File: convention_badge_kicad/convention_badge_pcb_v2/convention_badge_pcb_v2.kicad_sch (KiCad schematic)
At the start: 23 parts, among them J1 USBC, J2 ER-CON24HT-1, J3 3.7V Battery, SW1 SW4X2, SW2 SW4X2, SW4 SW_SPST, U1 ESP32-C3-WROOM-02, U3 TP4056

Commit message: schematic minus e paper integration complete
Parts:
- added C5: 0.1uF, PCM_JLCPCB:C_0603, symbol EESD:C
- added C6, C8: 2.2uF, PCM_JLCPCB:C_0603, symbol Device:C_Small_US
- added C7: 100uF, PCM_JLCPCB:C_0603, symbol Device:C_Small_US
- added C9: 0.1uF, PCM_JLCPCB:C_0603, symbol Device:C_Small_US
- added D3: SS14, PCM_JLCPCB:D_DO-214AC(SMA), symbol Device:D
- added Q1: LP0404N3T5G, Package_TO_SOT_SMD:SOT-883, symbol Simulation_SPICE:PMOS
- added R10: 100k, PCM_JLCPCB:R_0603, symbol Device:R_Small_US
- added R9: 1k, PCM_JLCPCB:R_0603, symbol Device:R_US
- added SW3, SW4, SW5, SW7, SW8: SW_Push, Button_Switch_THT:SW_PUSH_6mm, symbol Switch:SW_Push
- added U2: FS8205A, Package_TO_SOT_SMD:SOT-23-6, symbol 3_Battery_Managment:FS8205A
- added U4: DW01A, Package_TO_SOT_SMD:SOT-23-6, symbol 3_Battery_Managment:DW10A
- added U5: TLV75733PDBV, Package_TO_SOT_SMD:SOT-23-5, symbol Regulator_Linear:TLV75733PDBV
- C1, C2, C3, C4: footprint EESD:C0603 -> PCM_JLCPCB:C_0603
- D1, D2: footprint (none) -> PCM_JLCPCB:D_0603
- DISP1: renamed from DISP; value EPaper Display -> EPaper Breakout
- J1: footprint (none) -> Connector_USB:USB_C_Receptacle_GCT_USB4105-xx-A_16P_TopMnt_Horizontal
- J2: value ER-CON24HT-1 -> EPaper
- R1, R2: footprint EESD:R0603 -> PCM_JLCPCB:R_0603
- R3, R4, R5, R6, R8: footprint (none) -> PCM_JLCPCB:R_0603
- R7: value 1.2k -> 10k; footprint (none) -> PCM_JLCPCB:R_0603
- SW1, SW2: footprint EESD:PB4X2 -> PCM_JLCPCB:SW-SMD_4P-L5.1-W5.1-P3.70-LS6.5-TL-2
- renumbered SW4 to SW6
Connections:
- net +3.3V: now also C8.1, C9.1, U5.5 (OUT)
- net +3.7V: now also C4.1, R8.2, SW6.1 (A), U3.5 (BAT), Q1.1 (D); no longer J3.1 (Pin_1), SW6.2 (B)
- net EN: now also SW1.4; no longer SW1.2
- net GND: now also C4.2, SW1.2, SW2.2, C6.2, C7.2, C8.2, C9.2, R10.2, SW3.2, SW4.2, SW5.2, SW7.2, SW8.2, U5.2 (GND); no longer SW1.4, SW2.4
- net GPIO3: now also SW8.1
- net GPIO9: now also SW2.4; no longer SW2.2
- net VUSB: now also C7.1, D3.2 (A), Q1.2 (G), R10.1
- net at R8.1: now also C5.1, U4.5 (VCC)
- net GPIO20: now reaches U1.11 (GPIO20/U0RXD)
- net GPIO20: now also SW5.1
- net GPIO21: now reaches U1.12 (GPIO21/U0TXD)
- net GPIO21: now also SW7.1
- net GPIO1: now reaches U1.17 (GPIO1/ADC1_CH1/XTAL_32K_N)
- net GPIO1: now also SW4.1
- net GPIO0: now reaches U1.18 (GPIO0/ADC1_CH0/XTAL_32K_P)
- net GPIO0: now also SW3.1
- net at J3.2 (Pin_2): now also C5.2, U2.3 (S2), U4.6 (GND)
- new net: R9.1, U2.1 (S1)
- new net: R9.2, U4.2 (VM)
- new net: C6.1, D3.1 (K), Q1.3 (S), U5.1 (IN), U5.3 (EN)
- new net: J3.1 (Pin_1), SW6.2 (B)
- new net: U2.4 (G2), U4.1 (OD)
- new net: U2.6 (G1), U4.3 (OC)
- no-connect marks 2 -> 3
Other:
- moved on the sheet: C2, C4, DISP1, J2, J3, R4, R8, SW6

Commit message: layout is almost complete, kind of a rats nest
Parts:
- removed J2: EPaper, eastrising:ER-CON24HT-1, symbol eastrising:ER-EPD029-1_FPC
- removed SW7, SW8: SW_Push, Button_Switch_THT:SW_PUSH_6mm, symbol Switch:SW_Push
- added C10: 10uF, PCM_JLCPCB:C_0603, symbol Device:C_Small_US
- added D4, D5: LED, LED_THT:LED_D5.0mm, symbol Device:LED
- added J4, J5: Conn_01x10_Pin, Connector_PinHeader_2.54mm:PinHeader_1x10_P2.54mm_Vertical, symbol Connector:Conn_01x10_Pin
- added R11, R12: 1k, PCM_JLCPCB:R_0603, symbol Device:R_US
- R10: value 100k -> 10k
- R7: value 10k -> 2.2k
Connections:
- net +3.3V: now also C10.1, J4.1 (Pin_1), J4.10 (Pin_10)
- net EN: now also J4.2 (Pin_2)
- net GND: now also C10.2, J4.9 (Pin_9), R11.2, R12.2
- net GPIO0: now also D4.2 (A), J5.2 (Pin_2); no longer SW3.1
- net GPIO1: now also D5.2 (A), J5.3 (Pin_3); no longer SW4.1
- net GPIO10: now also SW5.1, J5.10 (Pin_10)
- net GPIO2: now also J5.4 (Pin_4)
- net GPIO20: now also SW4.1, J5.9 (Pin_9); no longer SW5.1
- net GPIO21: now also SW3.1, J5.8 (Pin_8)
- net GPIO3: now also J5.5 (Pin_5)
- net GPIO4: now also J4.3 (Pin_3)
- net GPIO5: now also J4.4 (Pin_4)
- net GPIO6: now also J4.5 (Pin_5)
- net GPIO7: now also J4.6 (Pin_6)
- net GPIO8: now also J4.7 (Pin_7)
- net GPIO9: now also J4.8 (Pin_8)
- net USB_D+: now also J5.6 (Pin_6)
- net USB_D-: now also J5.7 (Pin_7)
- net VUSB: now also J5.1 (Pin_1)
- net +3.7V renamed VBAT
- new net: D5.1 (K), R12.1
- new net: D4.1 (K), R11.1
- no-connect marks 3 -> 5
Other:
- moved on the sheet: C3, C4, C5, C6, C7, C8, C9, D1, D2, D3, DISP1, J3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

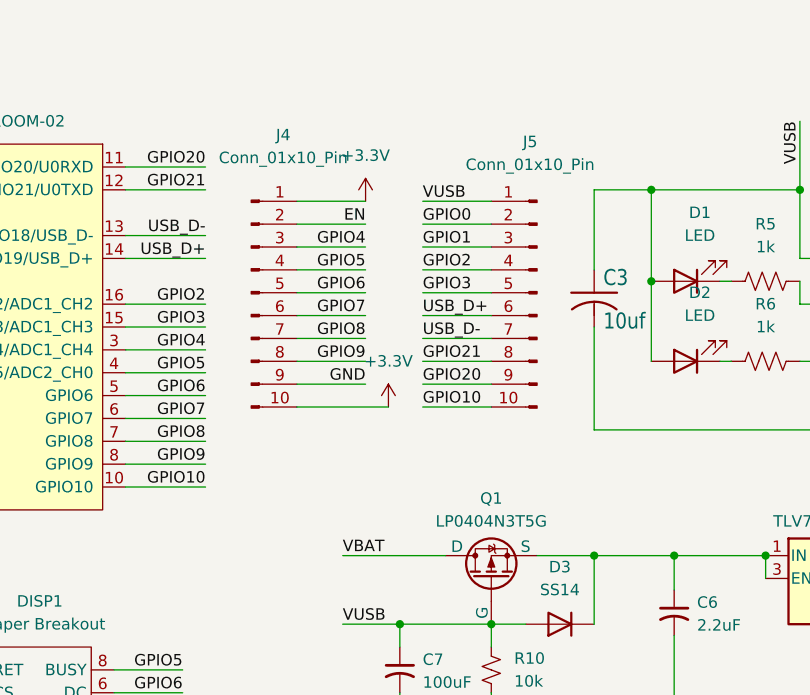
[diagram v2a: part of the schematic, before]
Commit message: cleaned up layout and seperated breakout headers.
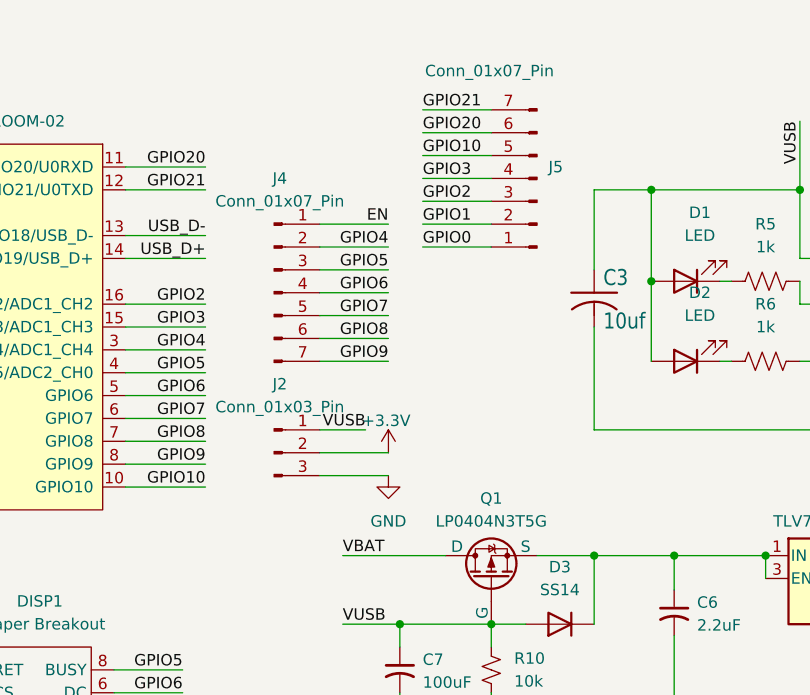
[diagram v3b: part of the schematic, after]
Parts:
- removed J4, J5: Conn_01x10_Pin, Connector_PinHeader_2.54mm:PinHeader_1x10_P2.54mm_Vertical, symbol Connector:Conn_01x10_Pin
- added J2: Conn_01x03_Pin, Connector_PinHeader_2.54mm:PinHeader_1x03_P2.54mm_Vertical, symbol Connector:Conn_01x03_Pin
- added J4, J5: Conn_01x07_Pin, Connector_PinHeader_2.54mm:PinHeader_1x07_P2.54mm_Vertical, symbol Connector:Conn_01x07_Pin
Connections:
- net +3.3V: now also J2.2 (Pin_2)
- net EN: now also J4.1 (Pin_1)
- net GND: now also J2.3 (Pin_3)
- net GPIO0: now also J5.1 (Pin_1)
- net GPIO1: now also J5.2 (Pin_2)
- net GPIO10: now also J5.5 (Pin_5)
- net GPIO2: now also J5.3 (Pin_3)
- net GPIO20: now also J5.6 (Pin_6)
- net GPIO21: now also J5.7 (Pin_7)
- net GPIO3: now also J5.4 (Pin_4)
- net GPIO4: now also J4.2 (Pin_2)
- net GPIO5: now also J4.3 (Pin_3)
- net GPIO6: now also J4.4 (Pin_4)
- net GPIO7: now also J4.5 (Pin_5)
- net GPIO8: now also J4.6 (Pin_6)
- net GPIO9: now also J4.7 (Pin_7)
- net VUSB: now also J2.1 (Pin_1)

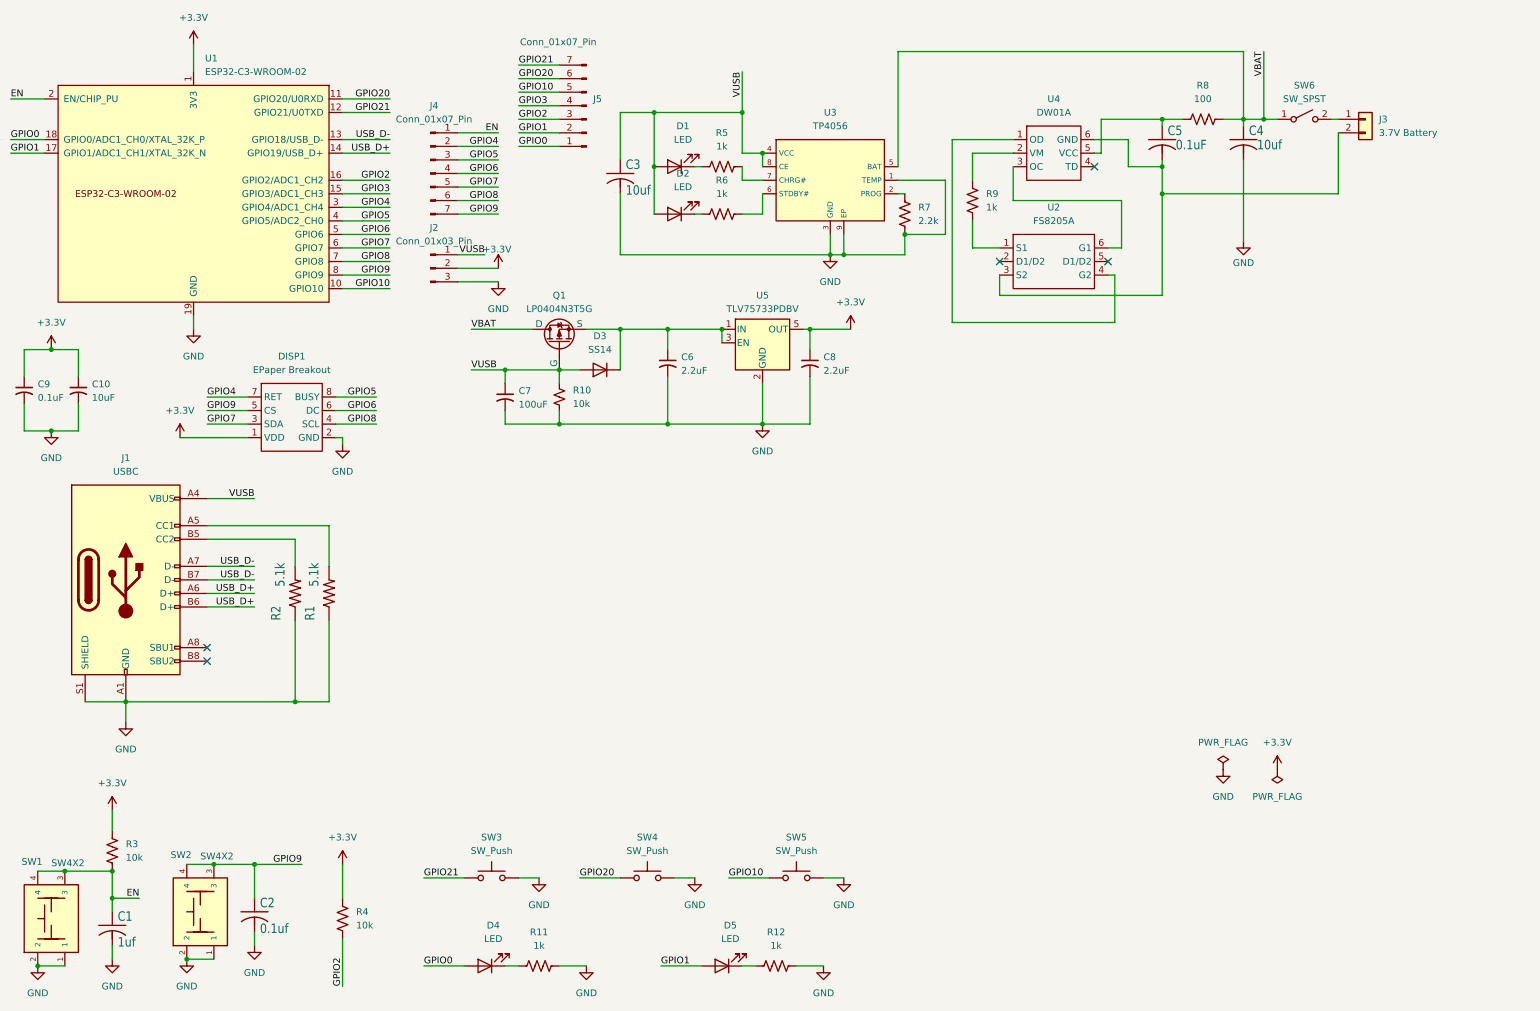
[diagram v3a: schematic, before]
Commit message: made board outline
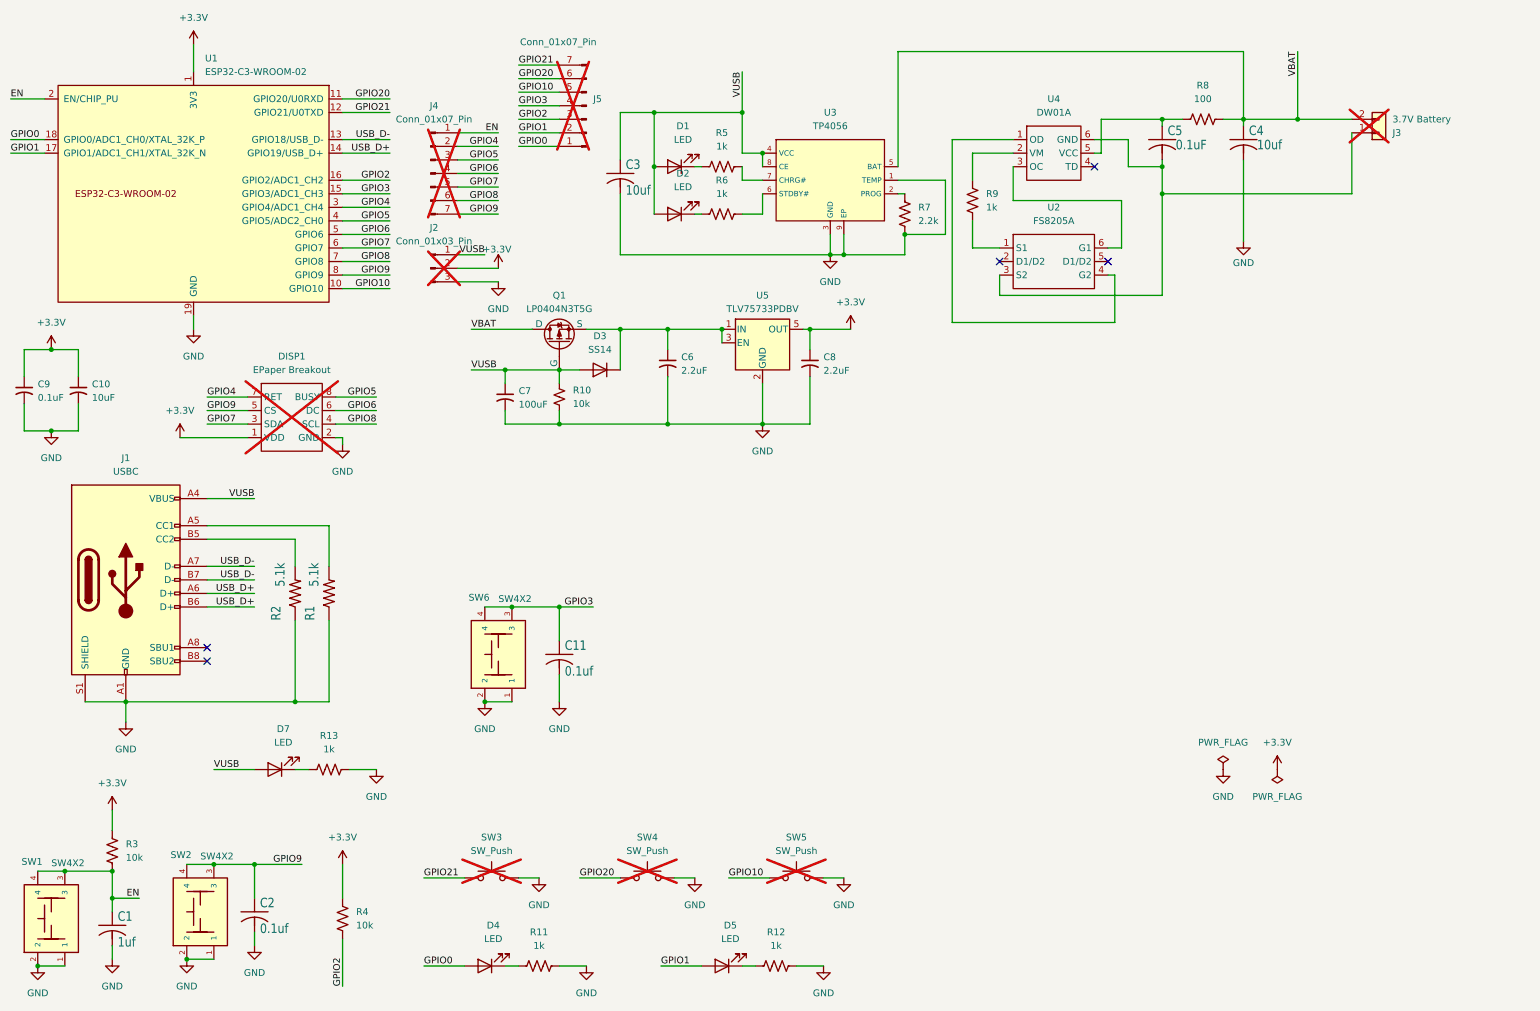
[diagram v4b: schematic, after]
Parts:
- removed SW6: SW_SPST, Button_Switch_THT:SW_Slide-03_Wuerth-WS-SLTV_10x2.5x6.4_P2.54mm, symbol Switch:SW_SPST
- added C11: 0.1uf, PCM_JLCPCB:C_0603, symbol EESD:C
- added D7: LED, PCM_JLCPCB:D_0603, symbol Device:LED
- added R13: 1k, PCM_JLCPCB:R_0603, symbol Device:R_US
- added SW6: SW4X2, PCM_JLCPCB:SW-SMD_4P-L5.1-W5.1-P3.70-LS6.5-TL-2, symbol EESD:KMR231GLFS
- DISP1, J2, J3, J4, J5, SW3, SW4, SW5: now not fitted
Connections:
- net GND: now also C11.2, R13.2, SW6.1, SW6.2
- net GPIO3: now also C11.1, SW6.3, SW6.4
- net VBAT: now also J3.2 (Pin_2)
- net VUSB: now also D7.2 (A)
- net at J3.1 (Pin_1): now also C5.2, U2.3 (S2), U4.6 (GND)
- new net: D7.1 (K), R13.1

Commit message: updated with part numbers and modified board to account for avail parts
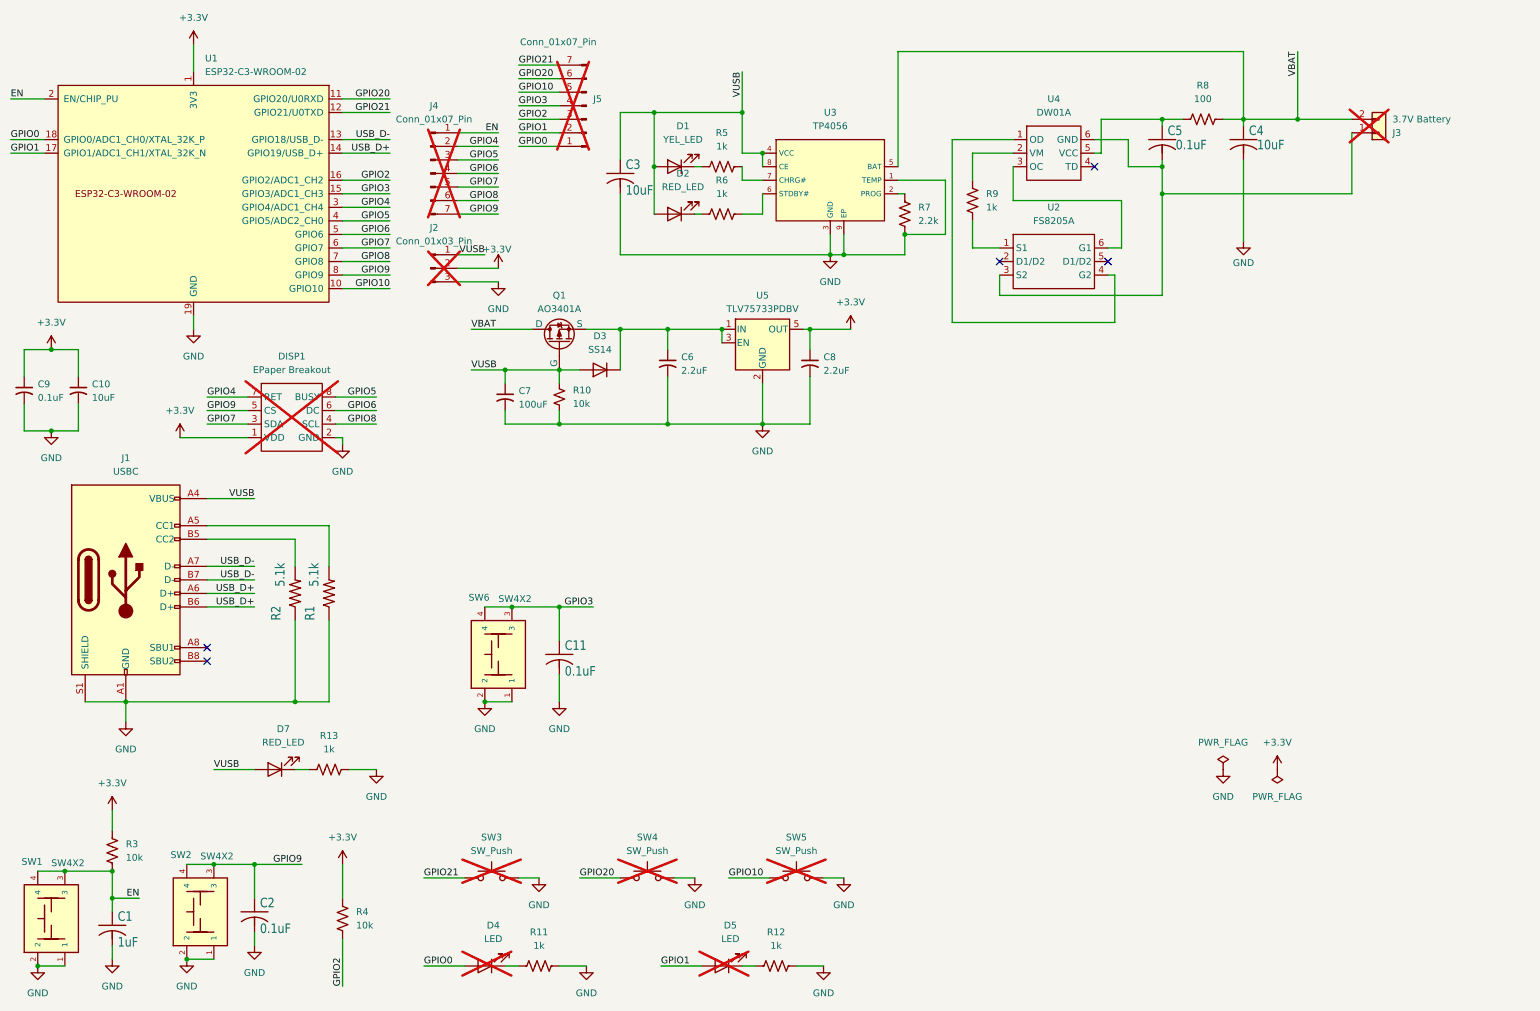
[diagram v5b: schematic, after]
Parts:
- C1: value 1uf -> 1uF; footprint PCM_JLCPCB:C_0603 -> Capacitor_SMD:C_0603_1608Metric; LCSC (none) -> C15849
- C10: footprint PCM_JLCPCB:C_0603 -> PCM_JLCPCB:C_CASE-A-3216-18(mm); LCSC (none) -> C7171
- C11, C2: value 0.1uf -> 0.1uF; footprint PCM_JLCPCB:C_0603 -> Capacitor_SMD:C_0603_1608Metric; LCSC (none) -> C1590
- C3, C4: value 10uf -> 10uF; footprint PCM_JLCPCB:C_0603 -> PCM_JLCPCB:C_CASE-A-3216-18(mm); LCSC (none) -> C7171
- C5, C9: footprint PCM_JLCPCB:C_0603 -> Capacitor_SMD:C_0603_1608Metric; LCSC (none) -> C1590
- C6, C8: footprint PCM_JLCPCB:C_0603 -> Capacitor_SMD:C_0603_1608Metric; LCSC (none) -> C1607
- C7: footprint PCM_JLCPCB:C_0603 -> PCM_JLCPCB:C_CASE-B-3528-21(mm); LCSC (none) -> C16133
- D1: value LED -> YEL_LED; LCSC (none) -> C2287
- D2, D7: value LED -> RED_LED; LCSC (none) -> C2286
- D3: LCSC (none) -> C2480
- D4, D5: now not fitted; now left out of the parts list
- DISP1, J2, J4, J5, SW3, SW4, SW5: now left out of the parts list
- J1: LCSC (none) -> C2765186
- J3: LCSC (none) -> C173752
- Q1: value LP0404N3T5G -> AO3401A; footprint Package_TO_SOT_SMD:SOT-883 -> Package_TO_SOT_SMD:SOT-23; LCSC (none) -> C20917
- R1, R2: LCSC (none) -> C23186
- R10, R3, R4: footprint PCM_JLCPCB:R_0603 -> Resistor_SMD:R_0805_2012Metric; LCSC (none) -> C17414
- R11, R12, R13, R5, R6, R9: LCSC (none) -> C21190
- R7: LCSC (none) -> C4190
- R8: LCSC (none) -> C22775
- SW1, SW2, SW6: LCSC (none) -> C318884
- U1: LCSC (none) -> C2944070
- U2: LCSC (none) -> C908265
- U4: LCSC (none) -> C351410
- U5: LCSC (none) -> C485517

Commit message: added solar pannel design, almost ready to order
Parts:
- C7: LCSC C16133 -> C122271
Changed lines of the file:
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@@
 			)
 		)
-		(property "LCSC" "C16133"
+		(property "LCSC" "C122271"
 			(at 107.95 85.09 0)
 			(effects

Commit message: submitted to jlcpcb
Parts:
- C11, C2, C5, C9: LCSC C1590 -> C14663
- C6, C8: LCSC C1607 -> C23630
- D1: LCSC C2287 -> C2290
- J2: LCSC (none) -> C2337
- SW1, SW2, SW6: LCSC C318884 -> C318884
- U4: LCSC C351410 -> C351410
- U5: LCSC C485517 -> C485517
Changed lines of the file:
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@@
 			)
 		)
-		(property "LCSC" " C485517"
+		(property "LCSC" "C485517"
 			(at 156.21 74.93 0)
 			(effects
@@
 			)
 		)
+		(property "LCSC" ""
+			(at 123.19 30.48 0)
+			(effects
+				(font
+					(size 1.27 1.27)
+				)
+				(hide yes)
+			)
+		)
 		(pin "1"
 		)
@@
 			)
 		)
+		(property "LCSC" "C2337"
+			(at 93.98 60.96 0)
+			(effects
+				(font
+					(size 1.27 1.27)
+				)
+				(hide yes)
+			)
+		)
 		(pin "1"
 		)
@@
 			)
 		)
-		(property "LCSC" "C1607"
+		(property "LCSC" "C23630"
 			(at 165.1 78.74 0)
 			(effects
@@
 			)
 		)
-		(property "LCSC" "C1590"
+		(property "LCSC" "C14663"
 			(at 231.14 36.83 0)
 			(effects
@@
 			)
 		)
-		(property "LCSC" " C318884"
+		(property "LCSC" "C318884"
 			(at 50.8 181.61 90)
 			(effects
@@
 			)
 		)
-		(property "LCSC" "C2287"
+		(property "LCSC" "C2290"
 			(at 139.7 41.91 0)
 			(effects
@@
 			)
 		)
-		(property "LCSC" " C318884"
+		(property "LCSC" "C318884"
 			(at 106.68 133.35 90)
 			(effects
@@
 			)
 		)
-		(property "LCSC" " C351410"
+		(property "LCSC" "C351410"
 			(at 210.82 39.37 0)
 			(effects
@@
 			)
 		)
+		(property "LCSC" ""
+			(at 93.98 43.18 0)
+			(effects
+				(font
+					(size 1.27 1.27)
+				)
+				(hide yes)
+			)
+		)
 		(pin "1"
 		)
@@
 			)
 		)
-		(property "LCSC" "C1590"
+		(property "LCSC" "C14663"
 			(at 17.78 83.82 0)
 			(effects
@@
 			)
 		)
-		(property "LCSC" "C1590"
+		(property "LCSC" "C14663"
 			(at 118.11 133.35 0)
 			(effects
@@
 			)
 		)
-		(property "LCSC" "C1590"
+		(property "LCSC" "C14663"
 			(at 60.96 181.61 0)
 			(effects
@@
 			)
 		)
-		(property "LCSC" "C1607"
+		(property "LCSC" "C23630"
 			(at 138.43 78.74 0)
 			(effects
@@
 			)
 		)
-		(property "LCSC" " C318884"
+		(property "LCSC" "C318884"
 			(at 22.86 182.88 90)
 			(effects
